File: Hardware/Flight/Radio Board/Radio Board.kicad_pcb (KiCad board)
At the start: 2 copper layers, 82 x 82 mm, 28 parts, among them J1 Conn_01x20_Female, J2 Conn_Coaxial, J3 Conn_Coaxial, U1 RFM95W-915S2, U2 RFM95W-915S2

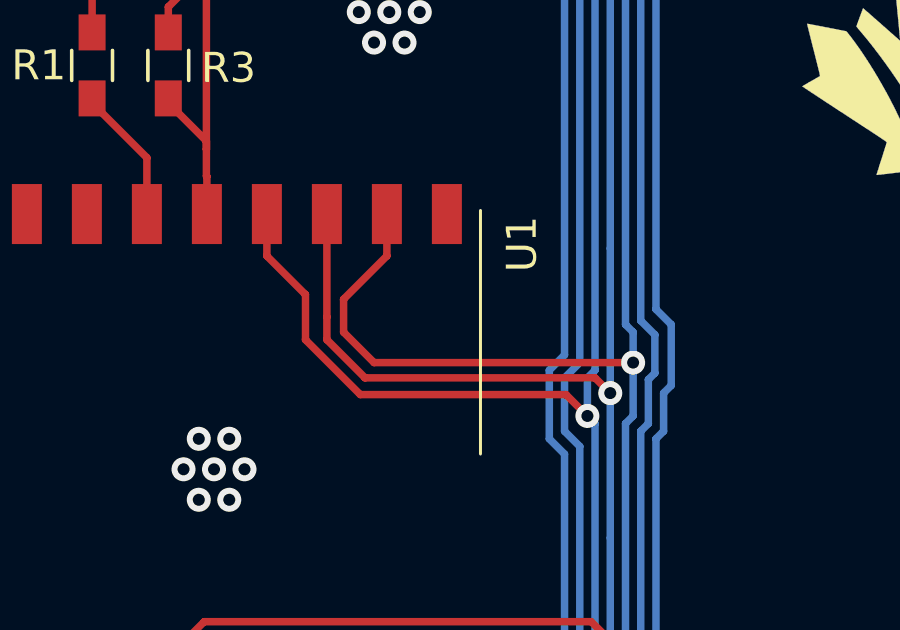
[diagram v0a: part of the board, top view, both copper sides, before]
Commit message: added battery board + ADCs for experiment board
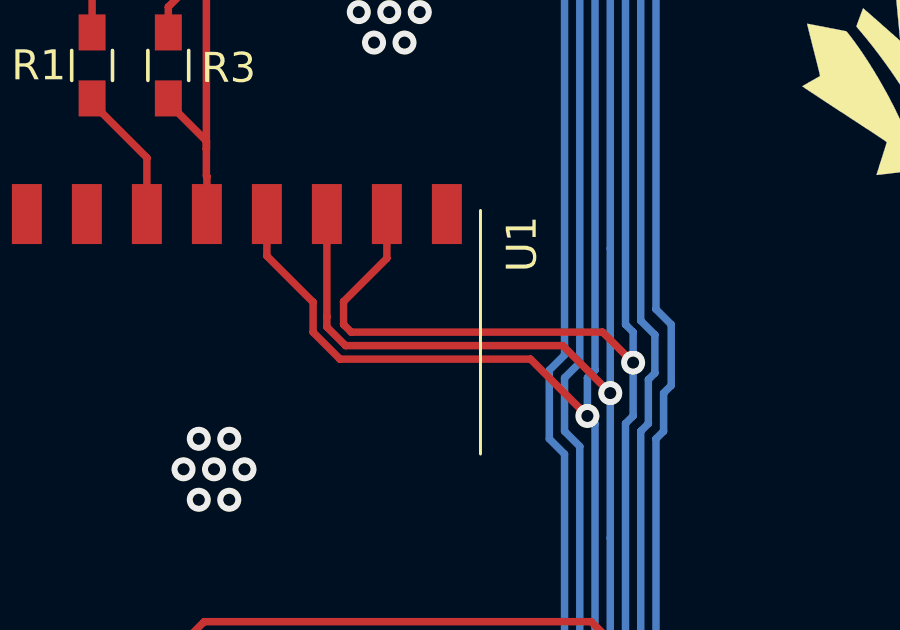
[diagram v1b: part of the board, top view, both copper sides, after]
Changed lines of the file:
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@@
     (thickness 1.6)
     (drawings 37)
-    (tracks 440)
+    (tracks 441)
     (zones 0)
     (modules 28)
@@
   (segment (start 13.208 50.038) (end 13.208 59.182) (width 0.25) (layer B.Cu) (net 12))
   (segment (start 24.622 26.924) (end 24.622 25.528) (width 0.25) (layer F.Cu) (net 12))
-  (segment (start 25.908 28.21) (end 24.622 26.924) (width 0.25) (layer F.Cu) (net 12))
-  (segment (start 25.908 29.718) (end 25.908 28.21) (width 0.25) (layer F.Cu) (net 12))
-  (segment (start 27.736011 31.546011) (end 25.908 29.718) (width 0.25) (layer F.Cu) (net 12))
-  (segment (start 34.594011 31.546011) (end 27.736011 31.546011) (width 0.25) (layer F.Cu) (net 12))
-  (segment (start 35.306 32.258) (end 34.594011 31.546011) (width 0.25) (layer F.Cu) (net 12))
+  (segment (start 26.162 28.464) (end 24.622 26.924) (width 0.25) (layer F.Cu) (net 12))
+  (segment (start 26.162 29.46682) (end 26.162 28.464) (width 0.25) (layer F.Cu) (net 12))
+  (segment (start 27.059198 30.364018) (end 26.162 29.46682) (width 0.25) (layer F.Cu) (net 12))
+  (segment (start 33.412019 30.364019) (end 27.059198 30.364018) (width 0.25) (layer F.Cu) (net 12))
+  (segment (start 35.306 32.258) (end 33.412019 30.364019) (width 0.25) (layer F.Cu) (net 12))
   (via (at 17.979044 60.038485) (size 0.8) (drill 0.4) (layers F.Cu B.Cu) (net 13))
   (segment (start 19.748485 60.038485) (end 19.814 60.104) (width 0.25) (layer F.Cu) (net 13))
@@
   (via (at 36.068 31.496) (size 0.8) (drill 0.4) (layers F.Cu B.Cu) (net 13))
   (segment (start 36.068 36.322) (end 36.068 31.496) (width 0.25) (layer B.Cu) (net 13))
-  (segment (start 26.622 28.956) (end 26.622 25.528) (width 0.25) (layer F.Cu) (net 13))
-  (segment (start 26.622 29.718) (end 26.622 28.956) (width 0.25) (layer F.Cu) (net 13))
-  (segment (start 27.892 30.988) (end 26.622 29.718) (width 0.25) (layer F.Cu) (net 13))
-  (segment (start 35.56 30.988) (end 27.892 30.988) (width 0.25) (layer F.Cu) (net 13))
-  (segment (start 36.068 31.496) (end 35.56 30.988) (width 0.25) (layer F.Cu) (net 13))
   (segment (start 36.068 31.496) (end 36.068 26.67) (width 0.25) (layer B.Cu) (net 13))
   (via (at 35.851 8.005653) (size 0.8) (drill 0.4) (layers F.Cu B.Cu) (net 13))
@@
   (segment (start 35.851 8.005653) (end 35.851 8.927) (width 0.25) (layer B.Cu) (net 13))
   (segment (start 36.068 26.67) (end 36.068 9.144) (width 0.25) (layer B.Cu) (net 13))
+  (segment (start 26.622 28.956) (end 26.622 25.528) (width 0.25) (layer F.Cu) (net 13))
+  (segment (start 26.622 29.29041) (end 26.622 28.956) (width 0.25) (layer F.Cu) (net 13))
+  (segment (start 27.245599 29.914009) (end 26.622 29.29041) (width 0.25) (layer F.Cu) (net 13))
+  (segment (start 34.48601 29.91401) (end 27.245599 29.914009) (width 0.25) (layer F.Cu) (net 13))
+  (segment (start 36.068 31.496) (end 34.48601 29.91401) (width 0.25) (layer F.Cu) (net 13))
   (via (at 17.979044 58.038485) (size 0.8) (drill 0.4) (layers F.Cu B.Cu) (net 14))
   (segment (start 19.748485 58.038485) (end 19.814 58.104) (width 0.25) (layer F.Cu) (net 14))
@@
   (segment (start 14.986 59.436) (end 16.581529 59.436) (width 0.25) (layer B.Cu) (net 14))
   (segment (start 16.002 48.768) (end 14.224 50.546) (width 0.25) (layer B.Cu) (net 14))
-  (segment (start 28.622 26.924) (end 28.622 25.528) (width 0.25) (layer F.Cu) (net 14))
-  (segment (start 27.178 28.368) (end 28.622 26.924) (width 0.25) (layer F.Cu) (net 14))
-  (segment (start 27.178 29.464) (end 27.178 28.368) (width 0.25) (layer F.Cu) (net 14))
-  (segment (start 28.194 30.48) (end 27.178 29.464) (width 0.25) (layer F.Cu) (net 14))
-  (segment (start 36.83 30.48) (end 28.194 30.48) (width 0.25) (layer F.Cu) (net 14))
+  (segment (start 28.622 27.004) (end 28.622 25.528) (width 0.25) (layer F.Cu) (net 14))
+  (segment (start 27.178 28.448) (end 28.622 27.004) (width 0.25) (layer F.Cu) (net 14))
+  (segment (start 27.178 29.21) (end 27.178 28.448) (width 0.25) (layer F.Cu) (net 14))
+  (segment (start 27.432 29.464) (end 27.178 29.21) (width 0.25) (layer F.Cu) (net 14))
+  (segment (start 36.83 30.48) (end 35.814 29.464) (width 0.25) (layer F.Cu) (net 14))
+  (segment (start 35.814 29.464) (end 27.432 29.464) (width 0.25) (layer F.Cu) (net 14))
   (segment (start 13.019255 41.497745) (end 12.988 41.529) (width 0.25) (layer F.Cu) (net 17))
   (segment (start 16.621 41.529) (end 16.622 41.528) (width 0.25) (layer F.Cu) (net 17))

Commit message: updated battery, experiment board. Added temp sensor to ARM board
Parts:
- J1: value Conn_01x20_Female -> Bus_Connector; footprint Pin_Headers:Pin_Header_Straight_2x10_Pitch2.54mm -> Payload_Connectors:Pin_Header_Straight_2x10_Pitch2.54mm
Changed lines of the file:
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@@
-    )
-  )
-  (module Pin_Headers:Pin_Header_Straight_2x10_Pitch2.54mm (layer F.Cu)
-    (at 29.57 5.54 90)
-    (descr "Through hole straight pin header, 2x10, 2.54mm pitch, double rows")
-    (tags "Through hole pin header THT 2x10 2.54mm double row")
-    (fp_text reference J1 (at 1.27 -2.33 180) (layer F.SilkS)
-      (effects (font (size 1 1) (thickness 0.15)))
-    )
-    (fp_text value Conn_01x20_Female (at 1.27 25.19 90) (layer F.Fab)
-      (effects (font (size 1 1) (thickness 0.15)))
-    )
-    (fp_text user %R (at 1.27 11.43 180) (layer F.Fab)
-      (effects (font (size 1 1) (thickness 0.15)))
-    )
-    (fp_line (start 4.35 -1.8) (end -1.8 -1.8) (layer F.CrtYd) (width 0.05))
-    (fp_line (start 4.35 24.65) (end 4.35 -1.8) (layer F.CrtYd) (width 0.05))
-    (fp_line (start -1.8 24.65) (end 4.35 24.65) (layer F.CrtYd) (width 0.05))
-    (fp_line (start -1.8 -1.8) (end -1.8 24.65) (layer F.CrtYd) (width 0.05))
-    (fp_line (start -1.33 -1.33) (end 0 -1.33) (layer F.SilkS) (width 0.12))
-    (fp_line (start -1.33 0) (end -1.33 -1.33) (layer F.SilkS) (width 0.12))
-    (fp_line (start 1.27 -1.33) (end 3.87 -1.33) (layer F.SilkS) (width 0.12))
-    (fp_line (start 1.27 1.27) (end 1.27 -1.33) (layer F.SilkS) (width 0.12))
-    (fp_line (start -1.33 1.27) (end 1.27 1.27) (layer F.SilkS) (width 0.12))
-    (fp_line (start 3.87 -1.33) (end 3.87 24.19) (layer F.SilkS) (width 0.12))
-    (fp_line (start -1.33 1.27) (end -1.33 24.19) (layer F.SilkS) (width 0.12))
-    (fp_line (start -1.33 24.19) (end 3.87 24.19) (layer F.SilkS) (width 0.12))
-    (fp_line (start -1.27 0) (end 0 -1.27) (layer F.Fab) (width 0.1))
-    (fp_line (start -1.27 24.13) (end -1.27 0) (layer F.Fab) (width 0.1))
-    (fp_line (start 3.81 24.13) (end -1.27 24.13) (layer F.Fab) (width 0.1))
-    (fp_line (start 3.81 -1.27) (end 3.81 24.13) (layer F.Fab) (width 0.1))
-    (fp_line (start 0 -1.27) (end 3.81 -1.27) (layer F.Fab) (width 0.1))
-    (pad 20 thru_hole oval (at 2.54 22.86 90) (size 1.7 1.7) (drill 1) (layers *.Cu *.Mask)
-      (net 3 "Net-(J1-Pad20)"))
-    (pad 19 thru_hole oval (at 0 22.86 90) (size 1.7 1.7) (drill 1) (layers *.Cu *.Mask)
-      (net 2 +3V3))
-    (pad 18 thru_hole oval (at 2.54 20.32 90) (size 1.7 1.7) (drill 1) (layers *.Cu *.Mask)
-      (net 4 "Net-(J1-Pad18)"))
-    (pad 17 thru_hole oval (at 0 20.32 90) (size 1.7 1.7) (drill 1) (layers *.Cu *.Mask)
-      (net 5 "Net-(J1-Pad17)"))
-    (pad 16 thru_hole oval (at 2.54 17.78 90) (size 1.7 1.7) (drill 1) (layers *.Cu *.Mask)
-      (net 6 "Net-(J1-Pad16)"))
-    (pad 15 thru_hole oval (at 0 17.78 90) (size 1.7 1.7) (drill 1) (layers *.Cu *.Mask)
-      (net 7 "Net-(J1-Pad15)"))
-    (pad 14 thru_hole oval (at 2.54 15.24 90) (size 1.7 1.7) (drill 1) (layers *.Cu *.Mask)
-      (net 27 "Net-(J1-Pad14)"))
-    (pad 13 thru_hole oval (at 0 15.24 90) (size 1.7 1.7) (drill 1) (layers *.Cu *.Mask)
-      (net 28 "Net-(J1-Pad13)"))
-    (pad 12 thru_hole oval (at 2.54 12.7 90) (size 1.7 1.7) (drill 1) (layers *.Cu *.Mask)
-      (net 29 "Net-(J1-Pad12)"))
-    (pad 11 thru_hole oval (at 0 12.7 90) (size 1.7 1.7) (drill 1) (layers *.Cu *.Mask)
-      (net 30 "Net-(J1-Pad11)"))
-    (pad 10 thru_hole oval (at 2.54 10.16 90) (size 1.7 1.7) (drill 1) (layers *.Cu *.Mask)
-      (net 10 CS2))
-    (pad 9 thru_hole oval (at 0 10.16 90) (size 1.7 1.7) (drill 1) (layers *.Cu *.Mask)
-      (net 11 CS1))
-    (pad 8 thru_hole oval (at 2.54 7.62 90) (size 1.7 1.7) (drill 1) (layers *.Cu *.Mask)
-      (net 12 SCK))
-    (pad 7 thru_hole oval (at 0 7.62 90) (size 1.7 1.7) (drill 1) (layers *.Cu *.Mask)
-      (net 13 MOSI))
-    (pad 6 thru_hole oval (at 2.54 5.08 90) (size 1.7 1.7) (drill 1) (layers *.Cu *.Mask)
-      (net 14 MISO))
-    (pad 5 thru_hole oval (at 0 5.08 90) (size 1.7 1.7) (drill 1) (layers *.Cu *.Mask)
-      (net 9 INT1))
-    (pad 4 thru_hole oval (at 2.54 2.54 90) (size 1.7 1.7) (drill 1) (layers *.Cu *.Mask)
-      (net 8 INT2))
-    (pad 3 thru_hole oval (at 0 2.54 90) (size 1.7 1.7) (drill 1) (layers *.Cu *.Mask)
-      (net 15 "Net-(J1-Pad3)"))
-    (pad 2 thru_hole oval (at 2.54 0 90) (size 1.7 1.7) (drill 1) (layers *.Cu *.Mask)
-      (net 16 "Net-(J1-Pad2)"))
-    (pad 1 thru_hole rect (at 0 0 90) (size 1.7 1.7) (drill 1) (layers *.Cu *.Mask)
-      (net 1 GND))
-    (model "D:/Tracked Repos/Payload 2019/Hardware/libs/Models/Connectors/ESQ-110-14-T-D.stp"
-      (offset (xyz 1.3 -11.5 2.5))
-      (scale (xyz 1 1 1))
-      (rotate (xyz -90 0 90))
     )
   )
@@
     )
   )
+  (module Payload_Connectors:Pin_Header_Straight_2x10_Pitch2.54mm (layer F.Cu)
+    (at 29.57 5.54 90)
+    (descr "Through hole straight pin header, 2x10, 2.54mm pitch, double rows")
+    (tags "Through hole pin header THT 2x10 2.54mm double row")
+    (fp_text reference J1 (at 1.27 -2.33 180) (layer F.SilkS)
+      (effects (font (size 1 1) (thickness 0.15)))
+    )
+    (fp_text value Bus_Connector (at 1.27 25.19 90) (layer F.Fab)
+      (effects (font (size 1 1) (thickness 0.15)))
+    )
+    (fp_text user %R (at 1.27 11.43 180) (layer F.Fab)
+      (effects (font (size 1 1) (thickness 0.15)))
+    )
+    (fp_line (start 4.35 -1.8) (end -1.8 -1.8) (layer F.CrtYd) (width 0.05))
+    (fp_line (start 4.35 24.65) (end 4.35 -1.8) (layer F.CrtYd) (width 0.05))
+    (fp_line (start -1.8 24.65) (end 4.35 24.65) (layer F.CrtYd) (width 0.05))
+    (fp_line (start -1.8 -1.8) (end -1.8 24.65) (layer F.CrtYd) (width 0.05))
+    (fp_line (start -1.33 -1.33) (end 0 -1.33) (layer F.SilkS) (width 0.12))
+    (fp_line (start -1.33 0) (end -1.33 -1.33) (layer F.SilkS) (width 0.12))
+    (fp_line (start 1.27 -1.33) (end 3.87 -1.33) (layer F.SilkS) (width 0.12))
+    (fp_line (start 1.27 1.27) (end 1.27 -1.33) (layer F.SilkS) (width 0.12))
+    (fp_line (start -1.33 1.27) (end 1.27 1.27) (layer F.SilkS) (width 0.12))
+    (fp_line (start 3.87 -1.33) (end 3.87 24.19) (layer F.SilkS) (width 0.12))
+    (fp_line (start -1.33 1.27) (end -1.33 24.19) (layer F.SilkS) (width 0.12))
+    (fp_line (start -1.33 24.19) (end 3.87 24.19) (layer F.SilkS) (width 0.12))
+    (fp_line (start -1.27 0) (end 0 -1.27) (layer F.Fab) (width 0.1))
+    (fp_line (start -1.27 24.13) (end -1.27 0) (layer F.Fab) (width 0.1))
+    (fp_line (start 3.81 24.13) (end -1.27 24.13) (layer F.Fab) (width 0.1))
+    (fp_line (start 3.81 -1.27) (end 3.81 24.13) (layer F.Fab) (width 0.1))
+    (fp_line (start 0 -1.27) (end 3.81 -1.27) (layer F.Fab) (width 0.1))
+    (pad 20 thru_hole oval (at 2.54 22.86 90) (size 1.7 1.7) (drill 1) (layers *.Cu *.Mask)
+      (net 3 "Net-(J1-Pad20)"))
+    (pad 19 thru_hole oval (at 0 22.86 90) (size 1.7 1.7) (drill 1) (layers *.Cu *.Mask)
+      (net 2 +3V3))
+    (pad 18 thru_hole oval (at 2.54 20.32 90) (size 1.7 1.7) (drill 1) (layers *.Cu *.Mask)
+      (net 4 "Net-(J1-Pad18)"))
+    (pad 17 thru_hole oval (at 0 20.32 90) (size 1.7 1.7) (drill 1) (layers *.Cu *.Mask)
+      (net 5 "Net-(J1-Pad17)"))
+    (pad 16 thru_hole oval (at 2.54 17.78 90) (size 1.7 1.7) (drill 1) (layers *.Cu *.Mask)
+      (net 6 "Net-(J1-Pad16)"))
+    (pad 15 thru_hole oval (at 0 17.78 90) (size 1.7 1.7) (drill 1) (layers *.Cu *.Mask)
+      (net 7 "Net-(J1-Pad15)"))
+    (pad 14 thru_hole oval (at 2.54 15.24 90) (size 1.7 1.7) (drill 1) (layers *.Cu *.Mask)
+      (net 27 "Net-(J1-Pad14)"))
+    (pad 13 thru_hole oval (at 0 15.24 90) (size 1.7 1.7) (drill 1) (layers *.Cu *.Mask)
+      (net 28 "Net-(J1-Pad13)"))
+    (pad 12 thru_hole oval (at 2.54 12.7 90) (size 1.7 1.7) (drill 1) (layers *.Cu *.Mask)
+      (net 29 "Net-(J1-Pad12)"))
+    (pad 11 thru_hole oval (at 0 12.7 90) (size 1.7 1.7) (drill 1) (layers *.Cu *.Mask)
+      (net 30 "Net-(J1-Pad11)"))
+    (pad 10 thru_hole oval (at 2.54 10.16 90) (size 1.7 1.7) (drill 1) (layers *.Cu *.Mask)
+      (net 10 CS2))
+    (pad 9 thru_hole oval (at 0 10.16 90) (size 1.7 1.7) (drill 1) (layers *.Cu *.Mask)
+      (net 11 CS1))
+    (pad 8 thru_hole oval (at 2.54 7.62 90) (size 1.7 1.7) (drill 1) (layers *.Cu *.Mask)
+      (net 12 SCK))
+    (pad 7 thru_hole oval (at 0 7.62 90) (size 1.7 1.7) (drill 1) (layers *.Cu *.Mask)
+      (net 13 MOSI))
+    (pad 6 thru_hole oval (at 2.54 5.08 90) (size 1.7 1.7) (drill 1) (layers *.Cu *.Mask)
+      (net 14 MISO))
+    (pad 5 thru_hole oval (at 0 5.08 90) (size 1.7 1.7) (drill 1) (layers *.Cu *.Mask)
+      (net 9 INT1))
+    (pad 4 thru_hole oval (at 2.54 2.54 90) (size 1.7 1.7) (drill 1) (layers *.Cu *.Mask)
+      (net 8 INT2))
+    (pad 3 thru_hole oval (at 0 2.54 90) (size 1.7 1.7) (drill 1) (layers *.Cu *.Mask)
+      (net 15 "Net-(J1-Pad3)"))
+    (pad 2 thru_hole oval (at 2.54 0 90) (size 1.7 1.7) (drill 1) (layers *.Cu *.Mask)
+      (net 16 "Net-(J1-Pad2)"))
+    (pad 1 thru_hole rect (at 0 0 90) (size 1.7 1.7) (drill 1) (layers *.Cu *.Mask)
+      (net 1 GND))
+    (model "D:/Tracked Repos/Payload 2019/Hardware/libs/Models/Connectors/ESQ-110-14-T-D.stp"
+      (offset (xyz 1.3 -11.5 2.5))
+      (scale (xyz 1 1 1))
+      (rotate (xyz -90 0 90))
+    )
+  )

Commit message: addressed Alex's ARM review comments
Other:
- outline, holes or cut-outs redrawn
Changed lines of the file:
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@@
   (general
     (thickness 1.6)
-    (drawings 37)
+    (drawings 41)
     (tracks 441)
     (zones 0)
@@
     )
   )
+  (gr_arc (start 2 80) (end 0 80) (angle -90) (layer Edge.Cuts) (width 0.2))
+  (gr_arc (start 80 80) (end 80 82) (angle -90) (layer Edge.Cuts) (width 0.2))
+  (gr_arc (start 80 2) (end 82 2) (angle -90) (layer Edge.Cuts) (width 0.2))
+  (gr_arc (start 2 2) (end 2 0) (angle -90) (layer Edge.Cuts) (width 0.2))
   (gr_line (start 10.454 37.677) (end 12.454 37.677) (layer F.SilkS) (width 0.2))
   (gr_line (start 13.454 36.677) (end 13.454 32.677) (layer F.SilkS) (width 0.2))
@@
   (gr_line (start 46.508 71.874) (end 50.508 71.874) (layer F.SilkS) (width 0.2))
   (gr_line (start 45.508 68.874) (end 45.508 70.874) (layer F.SilkS) (width 0.2))
-  (gr_line (start 0 0) (end 0 82) (layer Edge.Cuts) (width 0.2))
-  (gr_line (start 0 82) (end 82 82) (layer Edge.Cuts) (width 0.2))
-  (gr_line (start 82 48.5) (end 82 82) (layer Edge.Cuts) (width 0.2))
+  (gr_line (start 0 2) (end 0 80) (layer Edge.Cuts) (width 0.2))
+  (gr_line (start 2 82) (end 80 82) (layer Edge.Cuts) (width 0.2))
+  (gr_line (start 82 48.5) (end 82 80) (layer Edge.Cuts) (width 0.2))
   (gr_line (start 67 48.5) (end 82 48.5) (layer Edge.Cuts) (width 0.2))
   (gr_line (start 67 33.5) (end 67 48.5) (layer Edge.Cuts) (width 0.2))
   (gr_line (start 67 33.5) (end 82 33.5) (layer Edge.Cuts) (width 0.2))
-  (gr_line (start 82 0) (end 82 33.5) (layer Edge.Cuts) (width 0.2))
-  (gr_line (start 0 0) (end 82 0) (layer Edge.Cuts) (width 0.2))
+  (gr_line (start 82 2) (end 82 33.5) (layer Edge.Cuts) (width 0.2))
+  (gr_line (start 2 0) (end 80 0) (layer Edge.Cuts) (width 0.2))
   (gr_text "0.6mm thick, 4.4 permeability" (at 101.6 30.48) (layer F.Fab)
     (effects (font (size 1.5 1.5) (thickness 0.3)))
@@
     (polygon
       (pts
-        (xy 1.27 1.27) (xy 59.69 1.27) (xy 59.69 81.28) (xy 1.27 81.28)
+        (xy 0.508 0.508) (xy 59.69 0.508) (xy 59.69 81.534) (xy 0.508 81.534)
       )
     )
@@
     (polygon
       (pts
-        (xy 1.27 1.27) (xy 59.69 1.27) (xy 59.69 81.28) (xy 1.27 81.28)
+        (xy 0.508 0.508) (xy 59.69 0.508) (xy 59.69 81.534) (xy 0.508 81.534)
       )
     )

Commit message: addressing aarons comments for radio board
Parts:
- removed JP1, JP2, JP3, JP4: Jumper, Jumper:SolderJumper-2_P1.3mm_Open_RoundedPad1.0x1.5mm
- moved D3 3.05 mm to (52.5, 42.4)
- moved D4 3.05 mm to (52.6, 54.6)
- moved R7 3.05 mm to (48.0, 42.4)
- moved R8 3.05 mm to (48.0, 54.6)
- moved D1 1.02 mm to (52.6, 46.5)
- moved D2 1.02 mm to (52.5, 50.5)
- moved R5 1.02 mm to (48.0, 46.5)
- moved R6 1.02 mm to (48.0, 50.5)
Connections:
- net CS1 renamed /~CS1
- net CS2 renamed /~CS2
- net MISO renamed /MISO
- net MOSI renamed /MOSI
- net SCK renamed /SCK
- J1 pad 4: INT2 -> /INT2
- J1 pad 5: INT1 -> /INT1
- R5 pad 2: Net-(JP1-Pad2) -> /INT1
- R6 pad 2: Net-(JP2-Pad2) -> /INT2
- R7 pad 2: Net-(JP3-Pad2) -> Net-(R7-Pad2)
- R8 pad 2: Net-(JP4-Pad2) -> Net-(R8-Pad2)
- U1 pad 11: Net-(JP3-Pad1) -> Net-(R7-Pad2)
- U1 pad 14: INT1 -> /INT1
- U2 pad 11: Net-(JP4-Pad1) -> Net-(R8-Pad2)
- U2 pad 14: INT2 -> /INT2
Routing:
- net /INT1: track 0.00 -> 86.2 mm, vias 0 -> 1
- net /INT2: track 0.00 -> 76.2 mm, vias 0 -> 1
- net INT1: track 74.6 -> 0.00 mm, vias 1 -> 0
- net INT2: track 66.5 -> 0.00 mm, vias 1 -> 0
- net Net-(R8-Pad2): track 0.00 -> 33.3 mm
- net Net-(R7-Pad2): track 0.00 -> 28.9 mm
- net Net-(JP4-Pad1): track 26.5 -> 0.00 mm
- net Net-(JP3-Pad1): track 24.5 -> 0.00 mm
- net Net-(JP4-Pad2): track 4.66 -> 0.00 mm
- net Net-(JP3-Pad2): track 4.66 -> 0.00 mm
- net Net-(JP2-Pad2): track 4.45 -> 0.00 mm
- net Net-(JP1-Pad2): track 4.45 -> 0.00 mm
- net GND: vias 143 -> 150
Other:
- net class Default: clearance 0.2 -> 0
- rule trace_clearance: 0.2 -> 0
